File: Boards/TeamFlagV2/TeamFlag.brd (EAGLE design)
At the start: 46.2 x 47.5 mm, 12 parts

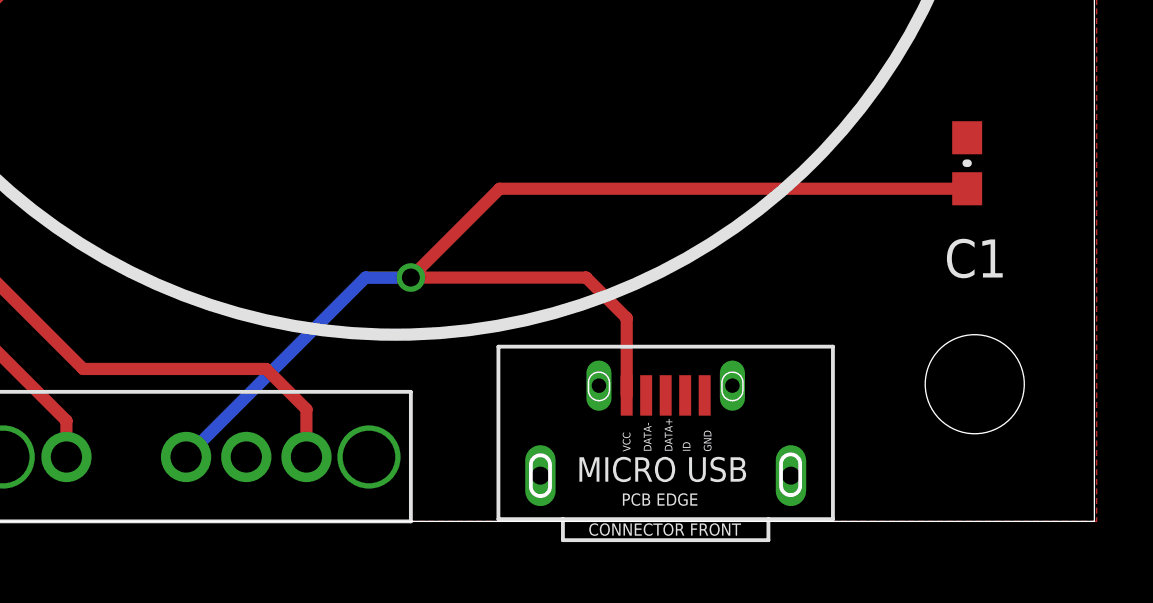
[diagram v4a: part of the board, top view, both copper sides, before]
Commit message: team flag fixed <3 margo
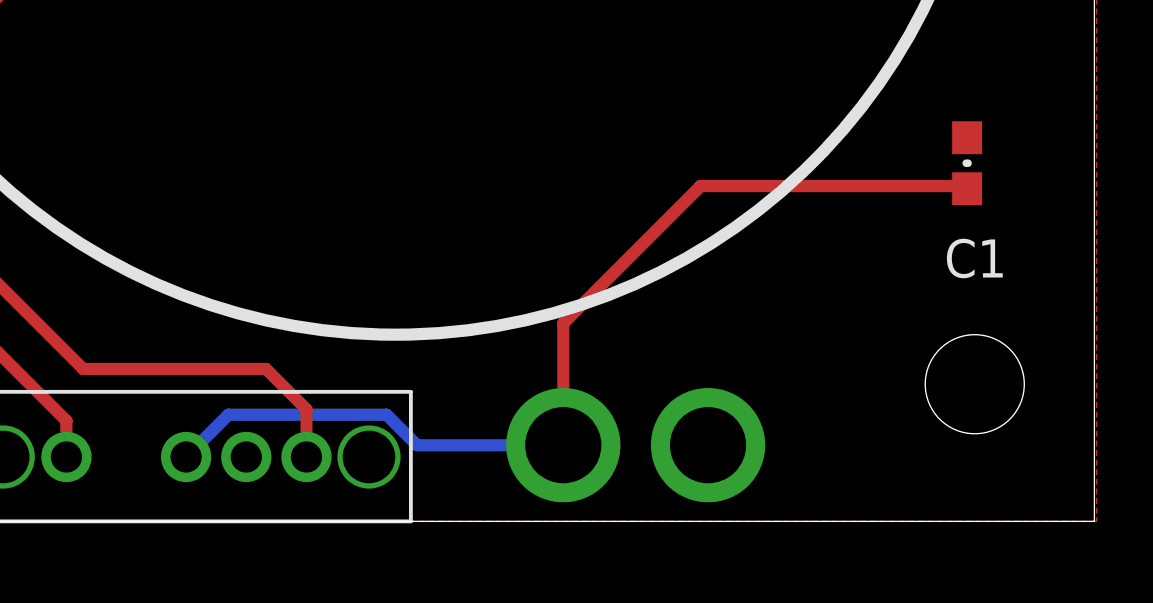
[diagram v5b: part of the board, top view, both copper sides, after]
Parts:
- removed U$1: MICRO_USB, pie:MICRO_USB
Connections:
- net GND: no longer U$1.GND
- net VCC: no longer U$1.VCC
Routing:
- net VCC: track 40.1 -> 33.0 mm
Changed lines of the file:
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@@
 <?xml version="1.0" encoding="utf-8"?>
 <!DOCTYPE eagle SYSTEM "eagle.dtd">
-<eagle version="7.6.0">
+<eagle version="8.2.2">
 <drawing>
 <settings>
@@
 <elements>
 <element name="C1" library="pie" package="0603-CAP" value="0.1uF" x="41.91" y="11.938" smashed="yes" rot="R270">
+<attribute name="NAME" x="41.148" y="8.128" size="1.27" layer="25" font="vector" ratio="10"/>
 <attribute name="PIE-INT-REF-NUM" value="CAPACITOR-GENERIC" x="41.91" y="11.938" size="1.778" layer="27" rot="R270" display="off"/>
-<attribute name="NAME" x="41.148" y="8.128" size="1.27" layer="25" font="vector" ratio="10"/>
 <attribute name="VALUE" x="40.386" y="14.478" size="1.27" layer="27" font="vector"/>
 </element>
@@
 </element>
 <element name="R1" library="pie" package="R0603" value="130" x="2.54" y="11.684" smashed="yes" rot="R270">
-<attribute name="MANUFACTURER_PART_NUMBER" value="" x="2.54" y="11.684" size="1.778" layer="27" rot="R270" display="off"/>
-<attribute name="NOTES" value="Cut Tape" x="2.54" y="11.684" size="1.778" layer="27" rot="R270" display="off"/>
 <attribute name="DESCRIPTION" value="RESISTOR, American symbol" x="2.54" y="11.684" size="1.778" layer="27" rot="R270" display="off"/>
 <attribute name="DISTRIBUTOR" value="DigiKey" x="2.54" y="11.684" size="1.778" layer="27" rot="R270" display="off"/>
-<attribute name="PACKAGE" value="R0603" x="2.54" y="11.684" size="1.778" layer="27" rot="R270" display="off"/>
 <attribute name="DISTRIBUTOR_PART_NUMBER" value="" x="2.54" y="11.684" size="1.778" layer="27" rot="R270" display="off"/>
 <attribute name="MANUFACTURER" value="Rohm Semiconductor" x="2.54" y="11.684" size="1.778" layer="27" rot="R270" display="off"/>
+<attribute name="MANUFACTURER_PART_NUMBER" value="" x="2.54" y="11.684" size="1.778" layer="27" rot="R270" display="off"/>
 <attribute name="NAME" x="1.524" y="14.224" size="1.27" layer="25" font="vector" ratio="10"/>
+<attribute name="NOTES" value="Cut Tape" x="2.54" y="11.684" size="1.778" layer="27" rot="R270" display="off"/>
+<attribute name="PACKAGE" value="R0603" x="2.54" y="11.684" size="1.778" layer="27" rot="R270" display="off"/>
 <attribute name="VALUE" x="0.762" y="8.128" size="1.27" layer="27" font="vector"/>
 </element>
 <element name="R2" library="pie" package="R0603" value="130" x="5.842" y="11.684" smashed="yes" rot="R270">
-<attribute name="MANUFACTURER_PART_NUMBER" value="" x="5.842" y="11.684" size="1.778" layer="27" rot="R270" display="off"/>
-<attribute name="NOTES" value="Cut Tape" x="5.842" y="11.684" size="1.778" layer="27" rot="R270" display="off"/>
 <attribute name="DESCRIPTION" value="RESISTOR, American symbol" x="5.842" y="11.684" size="1.778" layer="27" rot="R270" display="off"/>
 <attribute name="DISTRIBUTOR" value="DigiKey" x="5.842" y="11.684" size="1.778" layer="27" rot="R270" display="off"/>
-<attribute name="PACKAGE" value="R0603" x="5.842" y="11.684" size="1.778" layer="27" rot="R270" display="off"/>
 <attribute name="DISTRIBUTOR_PART_NUMBER" value="" x="5.842" y="11.684" size="1.778" layer="27" rot="R270" display="off"/>
 <attribute name="MANUFACTURER" value="Rohm Semiconductor" x="5.842" y="11.684" size="1.778" layer="27" rot="R270" display="off"/>
+<attribute name="MANUFACTURER_PART_NUMBER" value="" x="5.842" y="11.684" size="1.778" layer="27" rot="R270" display="off"/>
 <attribute name="NAME" x="4.826" y="14.224" size="1.27" layer="25" font="vector" ratio="10"/>
+<attribute name="NOTES" value="Cut Tape" x="5.842" y="11.684" size="1.778" layer="27" rot="R270" display="off"/>
+<attribute name="PACKAGE" value="R0603" x="5.842" y="11.684" size="1.778" layer="27" rot="R270" display="off"/>
 <attribute name="VALUE" x="4.572" y="8.128" size="1.27" layer="27" font="vector"/>
 </element>
-<element name="U$1" library="pie" package="MICRO_USB" value="MICRO_USB" x="27.686" y="1.524"/>
 <element name="U$3" library="pie" package="STAND-OFF" value="" x="4.064" y="42.672"/>
 <element name="U$4" library="pie" package="STAND-OFF" value="" x="42.164" y="42.672"/>
@@
 <contactref element="LED1" pad="K"/>
 <contactref element="LED2" pad="K"/>
-<contactref element="U$1" pad="GND"/>
 <polygon width="0.4064" layer="1">
 <vertex x="0" y="0"/>
@@
 </polygon>
 <contactref element="C1" pad="1"/>
+<via x="33.274" y="2.54" extent="1-16" drill="2.54"/>
 </signal>
 <signal name="N$2">
@@
 <signal name="VCC">
 <contactref element="C1" pad="2"/>
+<via x="28.448" y="2.54" extent="1-16" drill="2.54"/>
 <contactref element="U$2" pad="PIN2"/>
-<contactref element="U$1" pad="VCC"/>
-<wire x1="15.875" y1="2.1463" x2="21.8567" y2="8.128" width="0.4064" layer="16"/>
-<wire x1="21.8567" y1="8.128" x2="23.368" y2="8.128" width="0.4064" layer="16"/>
-<via x="23.368" y="8.128" extent="1-16" drill="0.6" shape="square"/>
-<wire x1="23.368" y1="8.128" x2="26.328" y2="11.088" width="0.4064" layer="1"/>
-<wire x1="26.328" y1="11.088" x2="41.91" y2="11.088" width="0.4064" layer="1"/>
-<wire x1="30.561" y1="4.199" x2="30.561" y2="6.777" width="0.4064" layer="1"/>
-<wire x1="30.561" y1="6.777" x2="29.21" y2="8.128" width="0.4064" layer="1"/>
-<wire x1="29.21" y1="8.128" x2="23.368" y2="8.128" width="0.4064" layer="1"/>
+<wire x1="28.448" y1="6.604" x2="28.448" y2="2.54" width="0.4064" layer="1"/>
+<wire x1="28.448" y1="6.604" x2="33.02" y2="11.176" width="0.4064" layer="1"/>
+<wire x1="33.02" y1="11.176" x2="41.822" y2="11.176" width="0.4064" layer="1"/>
+<wire x1="41.822" y1="11.176" x2="41.91" y2="11.088" width="0.4064" layer="1"/>
+<wire x1="28.448" y1="2.54" x2="23.57091875" y2="2.54" width="0.4064" layer="16"/>
+<wire x1="23.57091875" y1="2.54" x2="22.55491875" y2="3.556" width="0.4064" layer="16"/>
+<wire x1="22.55491875" y1="3.556" x2="17.2847" y2="3.556" width="0.4064" layer="16"/>
+<wire x1="17.2847" y1="3.556" x2="15.875" y2="2.1463" width="0.4064" layer="16"/>
 </signal>
 <signal name="PIN4">
